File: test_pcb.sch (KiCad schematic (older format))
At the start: 22 parts, among them J1 Conn_01x04_Male, J11 Conn_01x20_Female, J8 Conn_01x20_Female, SW1 on/off, SW2 on/off

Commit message: changes v2, ugly routing
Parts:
- removed led1: Led, Connector_PinSocket_2.54mm:PinSocket_1x02_P2.54mm_Vertical, symbol Connector:Conn_01x02_Female
- added mc2: Motors, Connector_PinSocket_2.54mm:PinSocket_1x06_P2.54mm_Vertical, symbol Connector:Conn_01x06_Female
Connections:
- net 5V: now also I2C1.2 (Pin_2), I2C2.2 (Pin_2), mc2.3 (Pin_3); no longer I2C1.1 (Pin_1), I2C2.1 (Pin_1)
- net GND: now also I2C1.1 (Pin_1), I2C2.1 (Pin_1), mc2.4 (Pin_4); no longer I2C1.2 (Pin_2), I2C2.2 (Pin_2)
- net a10: now also mc2.2 (Pin_2); no longer SRF2.2 (Pin_2)
- net a5: now also SRF1.2 (Pin_2)
- net a6: now also SRF1.3 (Pin_3)
- net a7: now also ENCB1.1 (Pin_1)
- net a9: now also mc2.5 (Pin_5); no longer SRF1.2 (Pin_2)
- net b1: now also mc2.1 (Pin_1); no longer IR1.3 (Pin_3)
- net b13: now also mc2.6 (Pin_6); no longer ENCB1.1 (Pin_1)
- net b8: now also SRF2.2 (Pin_2); no longer SRF1.3 (Pin_3)
- net c15: now also IR1.3 (Pin_3)

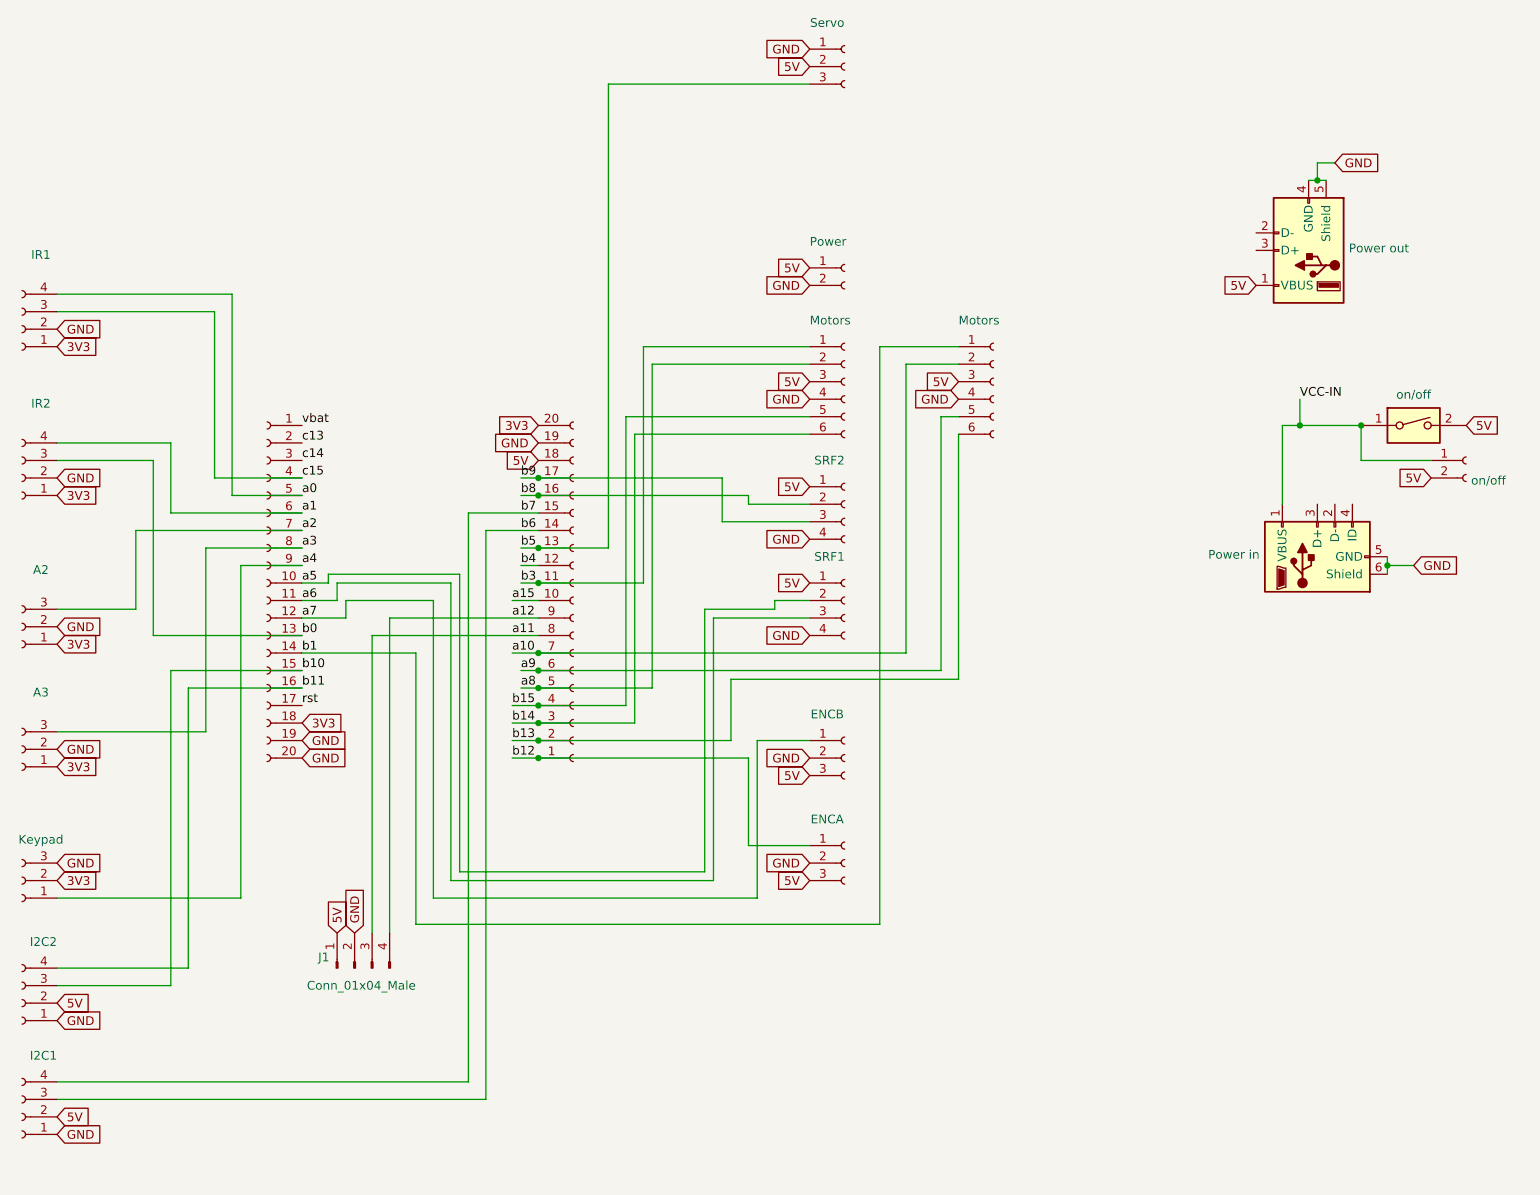
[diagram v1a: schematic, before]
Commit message: extra servo asssuming b5 works
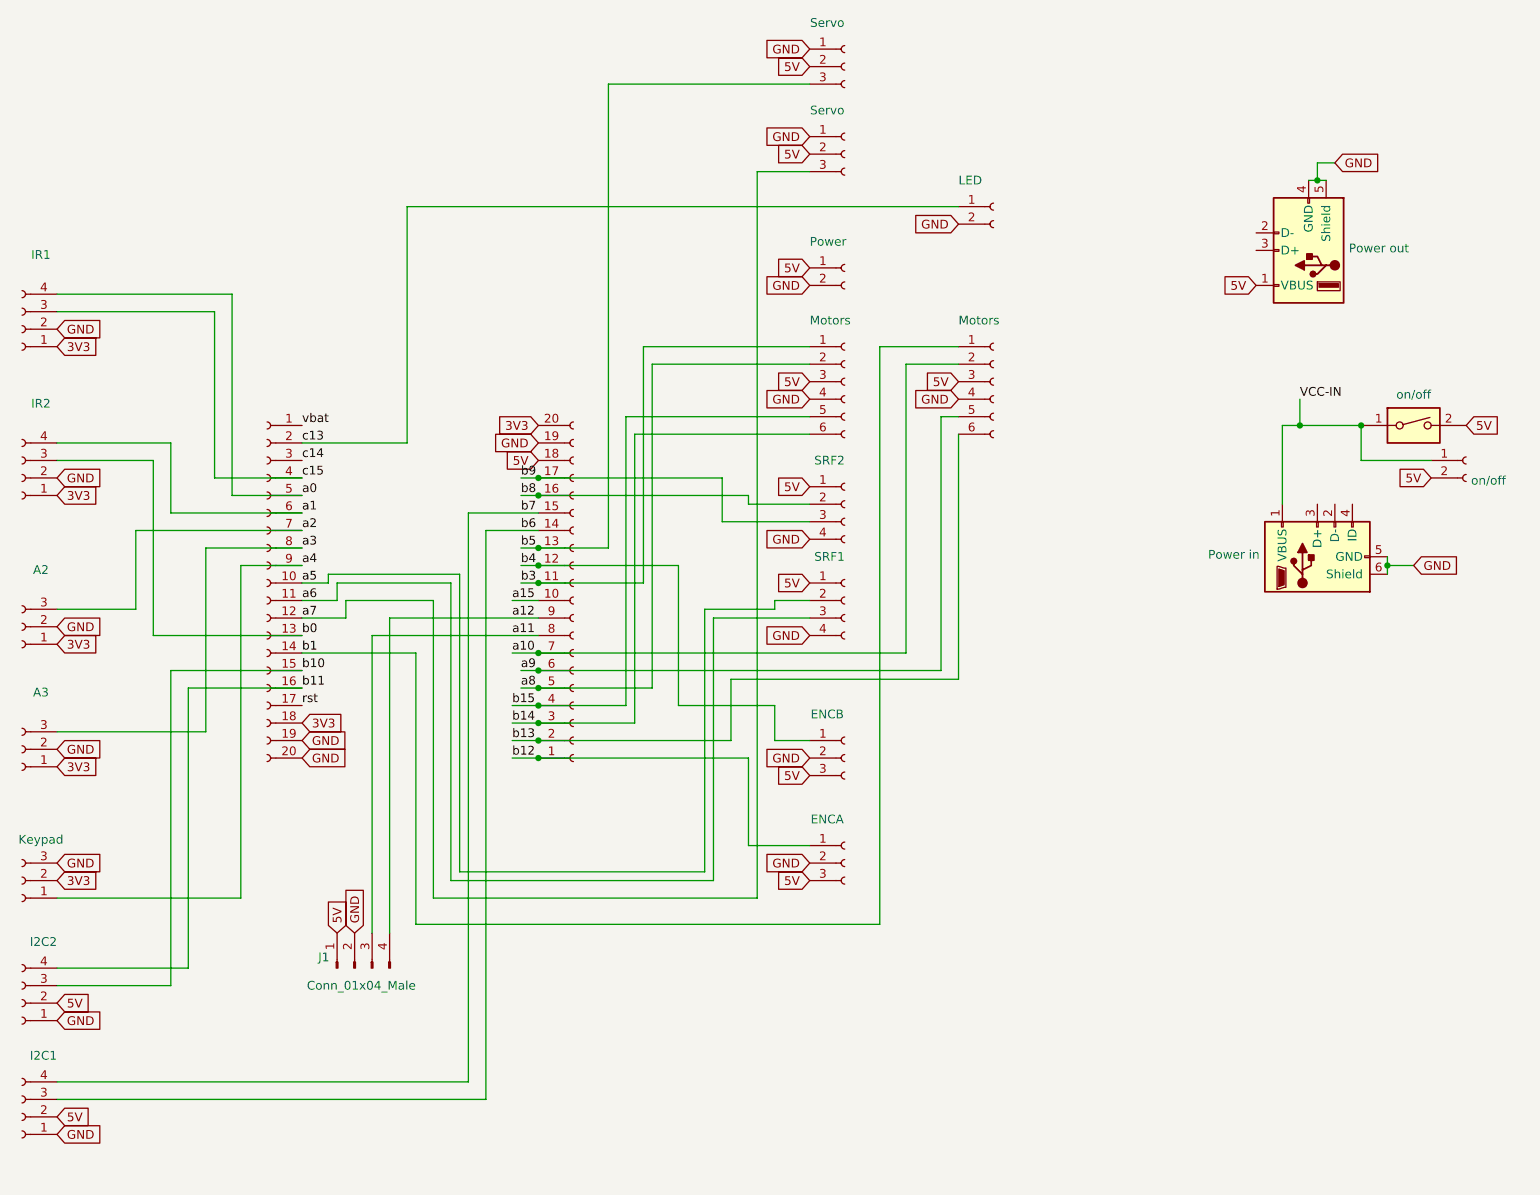
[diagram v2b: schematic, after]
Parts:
- added Power?: LED, Connector_PinHeader_2.54mm:PinHeader_1x02_P2.54mm_Vertical, symbol Connector:Conn_01x02_Female
- added Servo2: Servo, Connector_PinHeader_2.54mm:PinHeader_1x03_P2.54mm_Vertical, symbol Connector:Conn_01x03_Female
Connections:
- net 5V: now also Servo2.2 (Pin_2)
- net GND: now also Power?.2 (Pin_2), Servo2.1 (Pin_1)
- net a7: now also Servo2.3 (Pin_3); no longer ENCB1.1 (Pin_1)
- net b4: now also ENCB1.1 (Pin_1)
- net c13: now also Power?.1 (Pin_1)
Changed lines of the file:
@@
 Wire Wire Line
 	1900 6400 1150 6400
-Text GLabel 5450 1250 0    50   Input ~ 0
-5V
-Text GLabel 5450 1150 0    50   Input ~ 0
-GND
 $Comp
 L Connector:Conn_01x03_Female Servo1
@@
 $EndComp
 Wire Wire Line
-	4300 1350 5450 1350
-Wire Wire Line
 	4300 1350 4300 4000
 Wire Wire Line
@@
 Connection ~ 3900 4600
 Wire Wire Line
+	2550 4400 2800 4400
+Wire Wire Line
+	2800 4400 2800 4300
+Wire Wire Line
+	2800 4300 3300 4300
+Wire Wire Line
+	3300 4300 3300 6000
+Wire Wire Line
+	3300 6000 5150 6000
+Wire Wire Line
+	2550 4300 2750 4300
+Wire Wire Line
+	2750 4300 2750 4200
+Wire Wire Line
+	2750 4200 3400 4200
+Wire Wire Line
+	3400 4200 3400 5900
+Wire Wire Line
+	3400 5900 4900 5900
+Wire Wire Line
+	4900 5900 4900 4400
+Wire Wire Line
+	4900 4400 5450 4400
+Wire Wire Line
+	2550 4200 2700 4200
+Wire Wire Line
+	2700 4200 2700 4150
+Wire Wire Line
+	2700 4150 3450 4150
+Wire Wire Line
+	3450 4150 3450 5850
+Wire Wire Line
+	3450 5850 4850 5850
+Wire Wire Line
+	4850 5850 4850 4350
+Wire Wire Line
+	4850 4350 5250 4350
+Wire Wire Line
+	5250 4350 5250 4300
+Wire Wire Line
+	5250 4300 5450 4300
+Wire Wire Line
+	2550 4600 3200 4600
+Wire Wire Line
+	3200 4600 3200 6150
+Wire Wire Line
+	3200 6150 5850 6150
+Wire Wire Line
+	5850 6150 5850 2850
+Wire Wire Line
+	5850 2850 6300 2850
+Wire Wire Line
+	1150 2650 2050 2650
+Wire Wire Line
+	2050 2650 2050 3600
+Wire Wire Line
+	2050 3600 2550 3600
+$Comp
+L Connector:Conn_01x03_Female Servo2
+U 1 1 6015AEF9
+P 5650 1750
+F 0 "Servo2" V 5542 1425 50  0001 C CNN
+F 1 "Servo" H 5550 2000 50  0000 C CNN
+F 2 "Connector_PinHeader_2.54mm:PinHeader_1x03_P2.54mm_Vertical" H 5650 1750 50  0001 C CNN
+F 3 "~" H 5650 1750 50  0001 C CNN
+	1    5650 1750
+	1    0    0    -1
+$EndComp
+Wire Wire Line
+	4300 1350 5450 1350
+Text GLabel 5450 1150 0    50   Input ~ 0
+GND
+Text GLabel 5450 1250 0    50   Input ~ 0
+5V
+Text GLabel 5450 1650 0    50   Input ~ 0
+GND
+Text GLabel 5450 1750 0    50   Input ~ 0
+5V
+Wire Wire Line
+	5100 3750 5450 3750
+Wire Wire Line
+	5100 3700 5100 3750
+Connection ~ 3900 3700
+Wire Wire Line
 	3900 3700 5100 3700
 Wire Wire Line
-	5100 3700 5100 3750
-Wire Wire Line
-	5100 3750 5450 3750
-Connection ~ 3900 3700
-Wire Wire Line
-	2550 4400 2800 4400
-Wire Wire Line
-	2800 4400 2800 4300
-Wire Wire Line
-	2800 4300 3300 4300
-Wire Wire Line
-	3300 4300 3300 6000
-Wire Wire Line
-	3300 6000 5150 6000
-Wire Wire Line
-	5150 6000 5150 5100
-Wire Wire Line
-	5150 5100 5450 5100
-Wire Wire Line
-	2550 4300 2750 4300
-Wire Wire Line
-	2750 4300 2750 4200
-Wire Wire Line
-	2750 4200 3400 4200
-Wire Wire Line
-	3400 4200 3400 5900
-Wire Wire Line
-	3400 5900 4900 5900
-Wire Wire Line
-	4900 5900 4900 4400
-Wire Wire Line
-	4900 4400 5450 4400
-Wire Wire Line
-	2550 4200 2700 4200
-Wire Wire Line
-	2700 4200 2700 4150
-Wire Wire Line
-	2700 4150 3450 4150
-Wire Wire Line
-	3450 4150 3450 5850
-Wire Wire Line
-	3450 5850 4850 5850
-Wire Wire Line
-	4850 5850 4850 4350
-Wire Wire Line
-	4850 4350 5250 4350
-Wire Wire Line
-	5250 4350 5250 4300
-Wire Wire Line
-	5250 4300 5450 4300
-Wire Wire Line
-	2550 4600 3200 4600
-Wire Wire Line
-	3200 4600 3200 6150
-Wire Wire Line
-	3200 6150 5850 6150
-Wire Wire Line
-	5850 6150 5850 2850
-Wire Wire Line
-	5850 2850 6300 2850
-Wire Wire Line
-	1150 2650 2050 2650
-Wire Wire Line
-	2050 2650 2050 3600
-Wire Wire Line
-	2050 3600 2550 3600
+	5150 1850 5450 1850
+Wire Wire Line
+	5150 1850 5150 6000
+Wire Wire Line
+	5450 5100 5250 5100
+Wire Wire Line
+	5250 5100 5250 4900
+Wire Wire Line
+	5250 4900 4700 4900
+Wire Wire Line
+	4700 4900 4700 4100
+Wire Wire Line
+	4700 4100 3900 4100
+Connection ~ 3900 4100
+$Comp
+L Connector:Conn_01x02_Female Power?
+U 1 1 601D6728
+P 6500 2050
+F 0 "Power?" H 6528 2026 50  0001 L CNN
+F 1 "LED" H 6300 2200 50  0000 L CNN
+F 2 "Connector_PinHeader_2.54mm:PinHeader_1x02_P2.54mm_Vertical" H 6500 2050 50  0001 C CNN
+F 3 "~" H 6500 2050 50  0001 C CNN
+	1    6500 2050
+	1    0    0    -1
+$EndComp
+Text GLabel 6300 2150 0    50   Input ~ 0
+GND
+Wire Wire Line
+	2550 3400 3150 3400
+Wire Wire Line
+	3150 3400 3150 2050
+Wire Wire Line
+	3150 2050 6300 2050
 $EndSCHEMATC

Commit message: small text changes
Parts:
- added Power?: Power, Connector_PinSocket_2.54mm:PinSocket_1x02_P2.54mm_Vertical, symbol Connector:Conn_01x02_Female
- gave numbers to parts that had none: 1
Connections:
- net 5V: now also Power?.1 (Pin_1)
- net GND: now also Power?.2 (Pin_2)
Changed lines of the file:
@@
 Connection ~ 3900 4100
 $Comp
-L Connector:Conn_01x02_Female Power?
+L Connector:Conn_01x02_Female Power2
 U 1 1 601D6728
 P 6500 2050
-F 0 "Power?" H 6528 2026 50  0001 L CNN
+F 0 "Power2" H 6528 2026 50  0001 L CNN
 F 1 "LED" H 6300 2200 50  0000 L CNN
 F 2 "Connector_PinHeader_2.54mm:PinHeader_1x02_P2.54mm_Vertical" H 6500 2050 50  0001 C CNN
@@
 Wire Wire Line
 	3150 2050 6300 2050
+$Comp
+L Connector:Conn_01x02_Female Power?
+U 1 1 6021D8FD
+P 6250 2400
+F 0 "Power?" H 6278 2376 50  0001 L CNN
+F 1 "Power" H 6050 2550 50  0000 L CNN
+F 2 "Connector_PinSocket_2.54mm:PinSocket_1x02_P2.54mm_Vertical" H 6250 2400 50  0001 C CNN
+F 3 "~" H 6250 2400 50  0001 C CNN
+	1    6250 2400
+	1    0    0    -1
+$EndComp
+Text GLabel 6050 2400 0    50   Input ~ 0
+5V
+Text GLabel 6050 2500 0    50   Input ~ 0
+GND
 $EndSCHEMATC

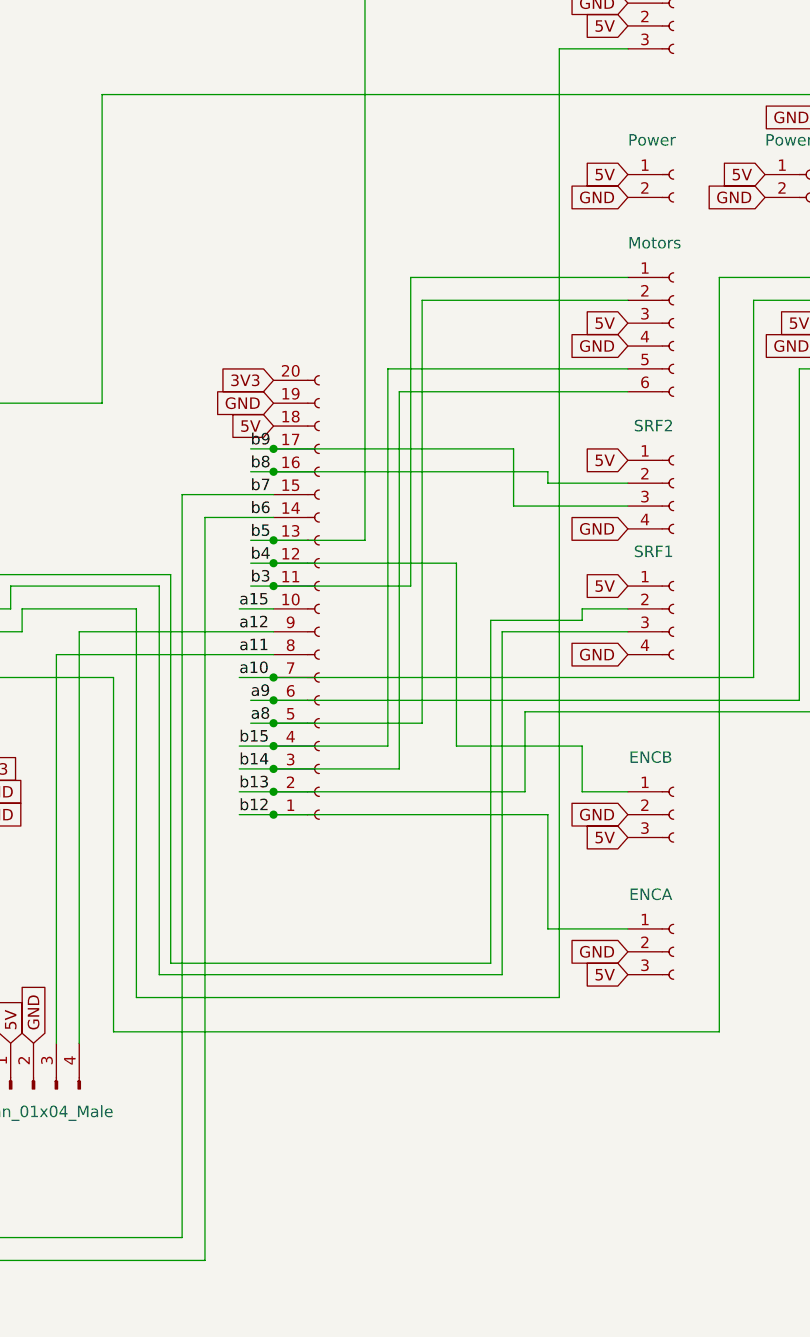
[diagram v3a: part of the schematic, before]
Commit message: switched i2c, added indicators bottom
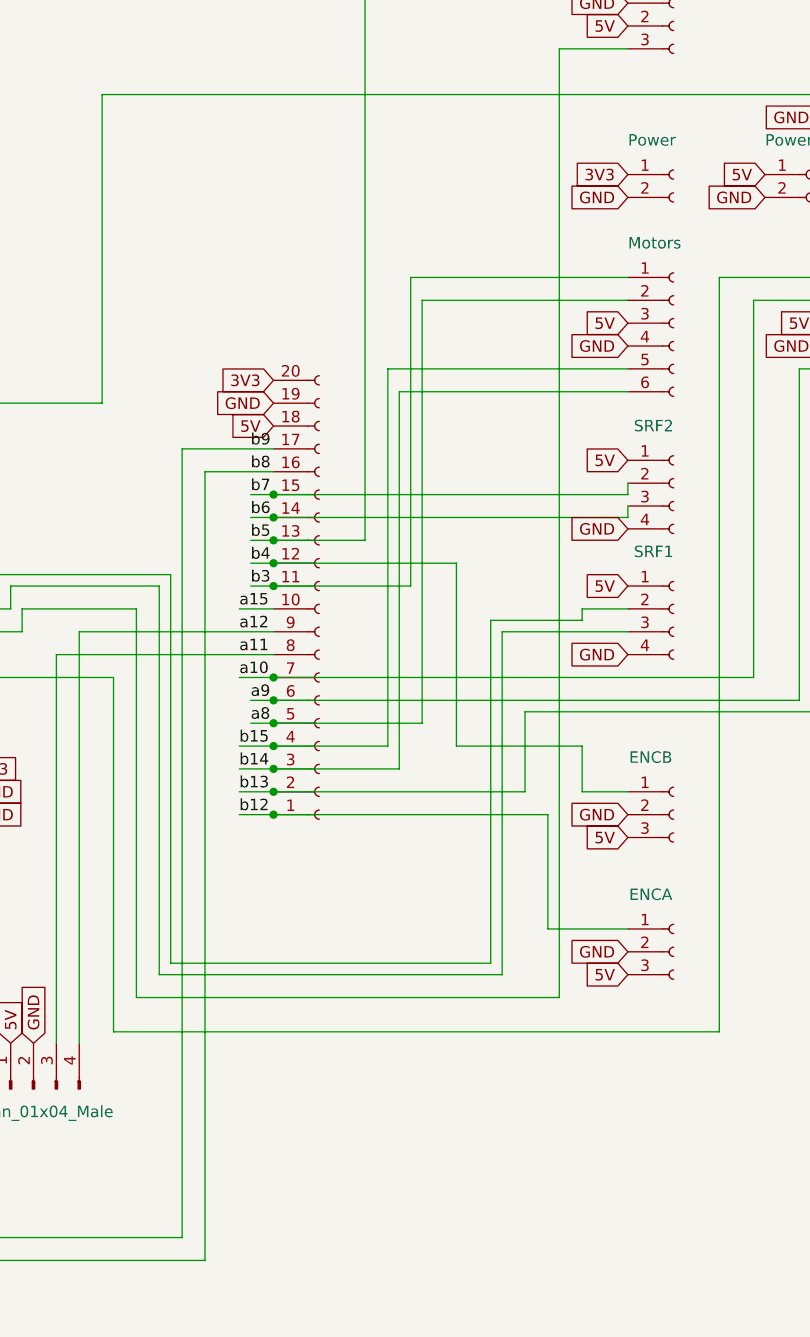
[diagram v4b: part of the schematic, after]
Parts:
- Power2: footprint Connector_PinHeader_2.54mm:PinHeader_1x02_P2.54mm_Vertical -> Connector_PinSocket_2.54mm:PinSocket_1x02_P2.54mm_Vertical
- gave numbers to parts that had none: 1
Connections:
- net 3V3: now also Power1.1 (Pin_1)
- net 5V: no longer Power1.1 (Pin_1)
- net b6: now also SRF2.3 (Pin_3); no longer I2C1.3 (Pin_3)
- net b7: now also SRF2.2 (Pin_2); no longer I2C1.4 (Pin_4)
- net b8: now also I2C1.3 (Pin_3); no longer SRF2.2 (Pin_2)
- net b9: now also I2C1.4 (Pin_4); no longer SRF2.3 (Pin_3)
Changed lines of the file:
@@
 	1150 6500 1800 6500
 Wire Wire Line
-	3500 3800 3500 7050
-Wire Wire Line
 	3500 7050 1150 7050
 Wire Wire Line
-	3900 3900 3600 3900
-Wire Wire Line
 	3600 7150 1150 7150
-Wire Wire Line
-	3600 3900 3600 7150
 Wire Wire Line
 	8750 4100 8900 4100
@@
 3V3
 Text GLabel 5450 3050 0    50   Input ~ 0
-5V
-Text GLabel 5450 2400 0    50   Input ~ 0
 5V
 Text GLabel 5450 3150 0    50   Input ~ 0
@@
 	0    -1   -1   0
 $EndComp
-Wire Wire Line
-	3900 3800 3500 3800
 Text Label 3800 3800 0    50   ~ 0
 b7
@@
 	4450 3350 4450 5000
 Wire Wire Line
-	5450 3850 4950 3850
-Wire Wire Line
 	3900 4800 4550 4800
 Wire Wire Line
 	4550 2950 4550 4800
-Wire Wire Line
-	3800 3600 3900 3600
 Wire Wire Line
 	3750 4300 3900 4300
@@
 Text GLabel 2850 6200 1    50   Input ~ 0
 GND
-Wire Wire Line
-	3800 3700 3900 3700
 Text GLabel 2550 5200 2    50   Input ~ 0
 GND
@@
 	8600 3500 8600 3300
 Connection ~ 8600 3300
-Wire Wire Line
-	3900 3600 4950 3600
-Wire Wire Line
-	4950 3600 4950 3850
-Connection ~ 3900 3600
 $Comp
 L Connector:Conn_01x06_Female mc2
@@
 5V
 Wire Wire Line
-	5100 3750 5450 3750
-Wire Wire Line
-	5100 3700 5100 3750
-Connection ~ 3900 3700
-Wire Wire Line
-	3900 3700 5100 3700
-Wire Wire Line
 	5150 1850 5450 1850
 Wire Wire Line
@@
 F 0 "Power2" H 6528 2026 50  0001 L CNN
 F 1 "LED" H 6300 2200 50  0000 L CNN
-F 2 "Connector_PinHeader_2.54mm:PinHeader_1x02_P2.54mm_Vertical" H 6500 2050 50  0001 C CNN
+F 2 "Connector_PinSocket_2.54mm:PinSocket_1x02_P2.54mm_Vertical" H 6500 2050 50  0001 C CNN
 F 3 "~" H 6500 2050 50  0001 C CNN
 	1    6500 2050
@@
 	3150 2050 6300 2050
 $Comp
-L Connector:Conn_01x02_Female Power?
+L Connector:Conn_01x02_Female Power3
 U 1 1 6021D8FD
 P 6250 2400
-F 0 "Power?" H 6278 2376 50  0001 L CNN
+F 0 "Power3" H 6278 2376 50  0001 L CNN
 F 1 "Power" H 6050 2550 50  0000 L CNN
 F 2 "Connector_PinSocket_2.54mm:PinSocket_1x02_P2.54mm_Vertical" H 6250 2400 50  0001 C CNN
@@
 Text GLabel 6050 2500 0    50   Input ~ 0
 GND
+Text GLabel 5450 2400 0    50   Input ~ 0
+3V3
+Wire Wire Line
+	3500 3600 3900 3600
+Wire Wire Line
+	3600 3700 3900 3700
+Wire Wire Line
+	3500 3600 3500 7050
+Wire Wire Line
+	3600 3700 3600 7150
+Wire Wire Line
+	5450 3800 5450 3750
+Wire Wire Line
+	5450 3900 5450 3850
+Wire Wire Line
+	3800 3900 3900 3900
+Connection ~ 3900 3900
+Wire Wire Line
+	3900 3900 5450 3900
+Wire Wire Line
+	3800 3800 3900 3800
+Connection ~ 3900 3800
+Wire Wire Line
+	3900 3800 5450 3800
 $EndSCHEMATC
